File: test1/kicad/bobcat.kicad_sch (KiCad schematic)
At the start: 9 parts, among them U1 Bobcat

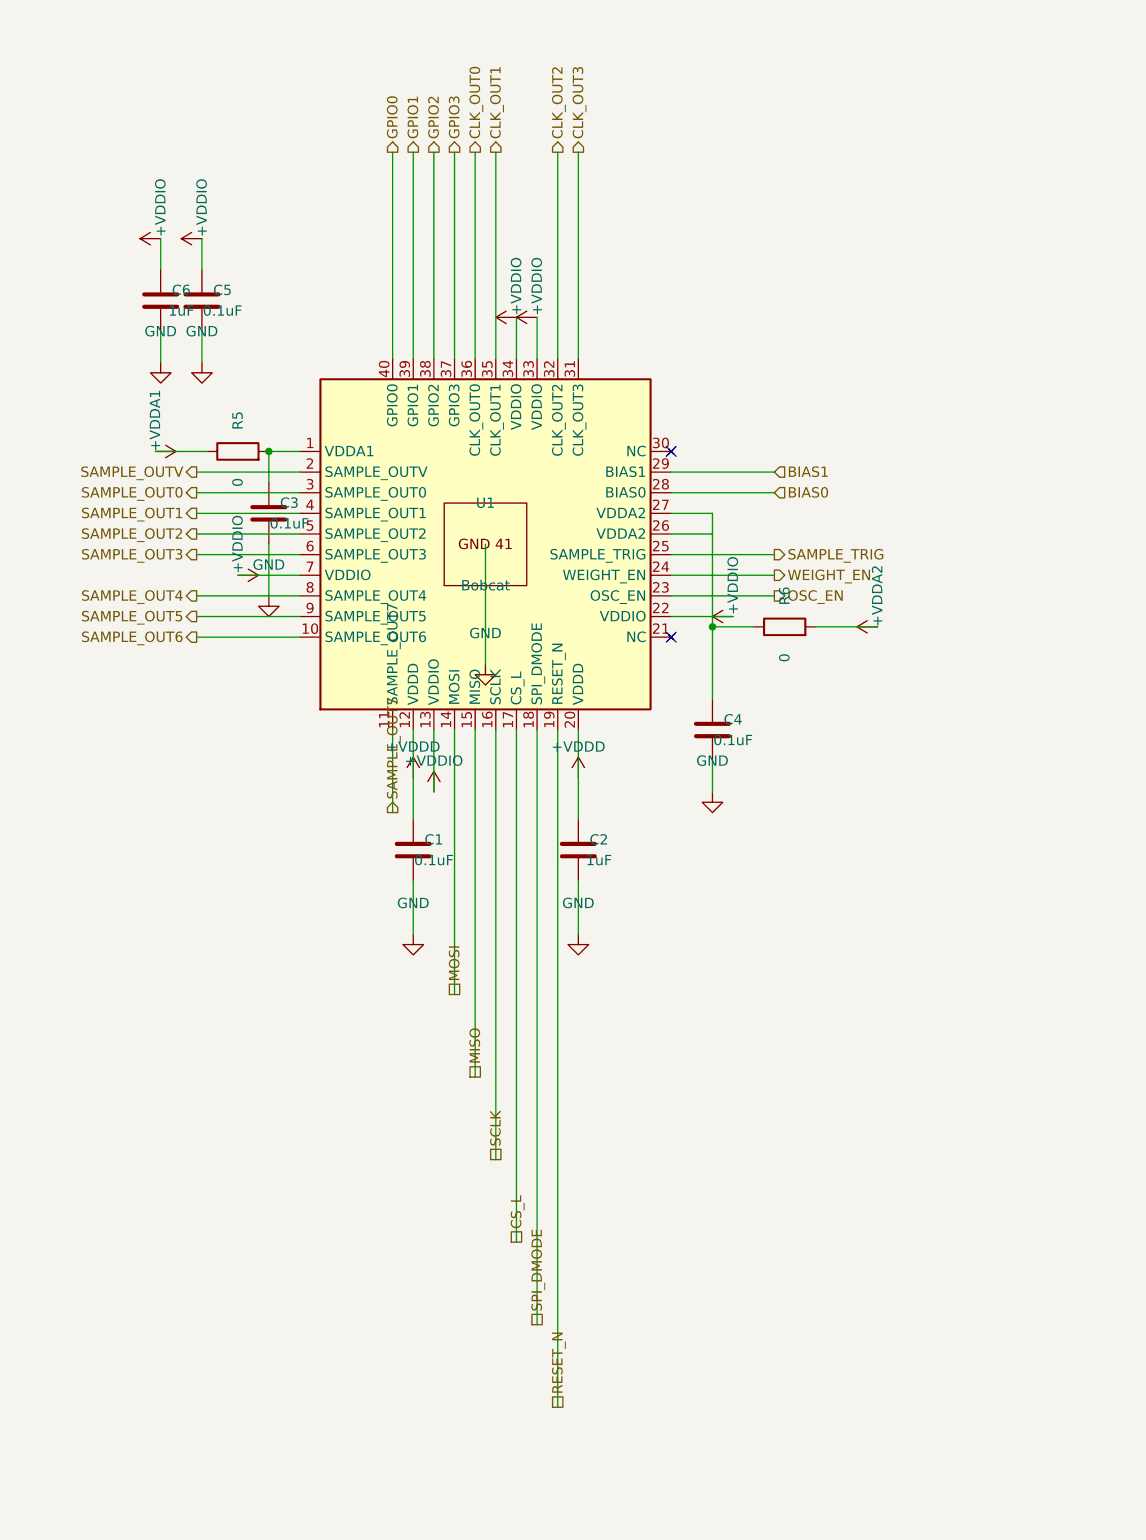
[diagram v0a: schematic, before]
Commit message: Project-wide connectivity audit: refdes uniqueness + hier-label correctness
Added test1/verify_project.py as a kicad-cli-erc substitute (the dev
build doesn't ship _cvpcb.kiface, so sch erc is broken). The verifier
parses all .kicad_sch files and checks:
  1. Duplicate refdes (KiCad's refdes namespace is project-wide).
  2. Parent sheet-pin name + direction matches child hierarchical_label.
  3. Orphan child hierarchical_labels (no matching parent pin).

First run flagged 48 issues. Now reports 0.

Refdes scheme — per-sheet decade ranges so global namespace stays unique:
  FMC 1-9 (J1-J4)
  Power 10-19 (U10/U11, R10/R11, C10-C16, J10-J12)
  Bobcat 20-29 (U20, R20/R21, C20-C25)
  EEPROM 30-39 (U30, R30/R31, C30)
  Bias 40-49 (U40/U41 [U41 dual-unit OPA], Q40-Q43, R40/R41, C40-C43)
  Connectors 50-59 (J50-J57, TP50-TP52)

Hierarchical / global label rework:
  - Parent sheet-pin directions corrected to match child labels (was
    flipped on every Bobcat SPI pin and on FMC's LDO_EN/LSW_EN/LDO_PG).
  - Bobcat SPI labels: passive → input/output as appropriate.
  - Project-wide nets converted to global_label (auto-tie by name, no
    parent pins): SCL, SDA, SAMPLE_OUT*, OSC_EN, WEIGHT_EN, SAMPLE_TRIG,
    BIAS_ISO0/1, CS_L, SCLK, MOSI, MISO, SPI_DMODE, RESET_N.
  - hier_label retained for clean 2-sheet pairs: VADJ, LDO_EN, LDO_PG,
    LSW_EN (FMC ↔ Power); BIAS0/1 (Bias ↔ Bobcat); CLK_OUT0-3, GPIO0-3
    (Bobcat ↔ Connectors).
  - Visual cue in renders: globals render as boxed rectangles; hierarchical
    labels render as arrows — handy when scanning a sheet.

Memory: appended five connectivity-correctness lessons to
feedback_kicad_generator_lessons.md (refdes namespace, parent/child
direction parity, no-passive-for-real-signals, global vs hier decision
table, verify-after-every-change).

Co-Authored-By: Claude Opus 4.7 (1M context) <noreply@anthropic.com>
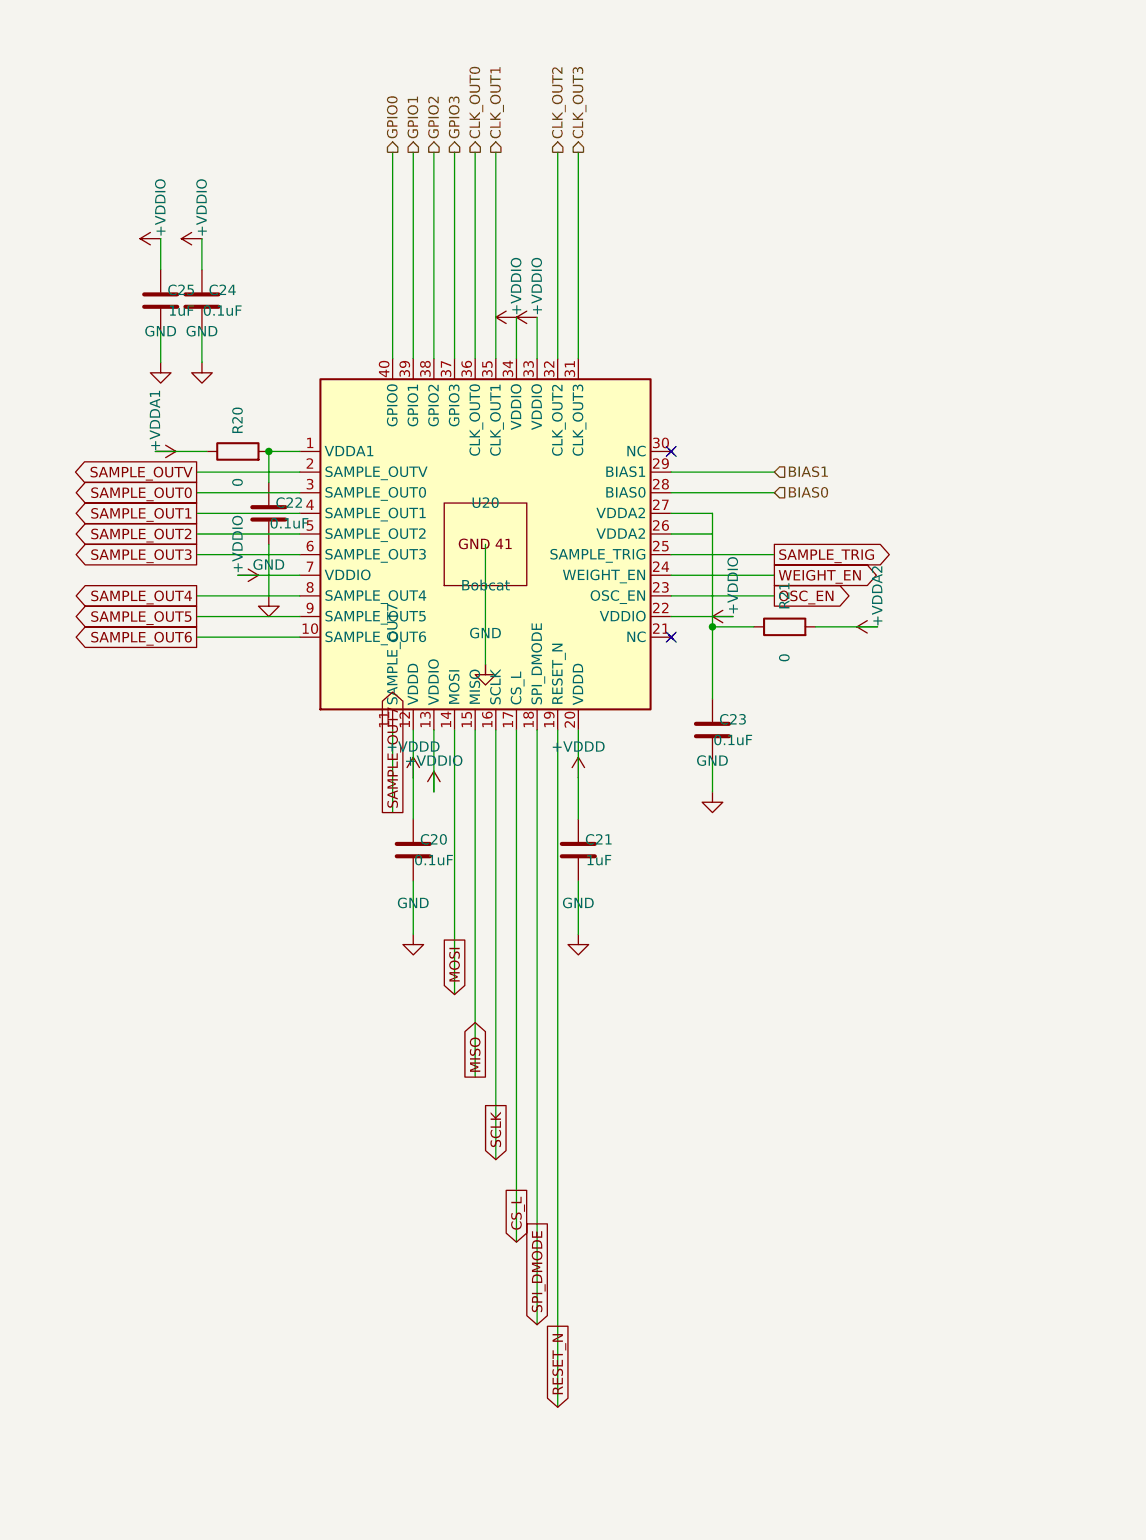
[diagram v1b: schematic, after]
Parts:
- removed C1, C3, C4, C5: 0.1uF, Capacitor_SMD:C_0402_1005Metric, symbol Device:C
- removed C2, C6: 1uF, Capacitor_SMD:C_0402_1005Metric, symbol Device:C
- removed R5, R6: 0, Resistor_SMD:R_0402_1005Metric, symbol Device:R
- removed U1: Bobcat, Bobcat:QFN-40_5x5mm_P0.4mm_EP3.5mm, symbol Lib:Bobcat
- added C20, C22, C23, C24: 0.1uF, Capacitor_SMD:C_0402_1005Metric, symbol Device:C
- added C21, C25: 1uF, Capacitor_SMD:C_0402_1005Metric, symbol Device:C
- added R20, R21: 0, Resistor_SMD:R_0402_1005Metric, symbol Device:R
- added U20: Bobcat, Bobcat:QFN-40_5x5mm_P0.4mm_EP3.5mm, symbol Lib:Bobcat
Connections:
- net +VDDA1: now also R20.1
- net +VDDA2: now also R21.2
- net +VDDD: now also C20.1, C21.1, U20.12 (VDDD), U20.20 (VDDD)
- net +VDDIO: now also C24.1, C25.1, U20.13 (VDDIO), U20.22 (VDDIO), U20.33 (VDDIO), U20.34 (VDDIO), U20.7 (VDDIO)
- net BIAS0: now also U20.28 (BIAS0)
- net BIAS1: now also U20.29 (BIAS1)
- net CLK_OUT0: now also U20.36 (CLK_OUT0)
- net CLK_OUT1: now also U20.35 (CLK_OUT1)
- net CLK_OUT2: now also U20.32 (CLK_OUT2)
- net CLK_OUT3: now also U20.31 (CLK_OUT3)
- net CS_L: now also U20.17 (CS_L)
- net GND: now also C20.2, C21.2, C22.2, C23.2, C24.2, C25.2, U20.41 (GND)
- net GPIO0: now also U20.40 (GPIO0)
- net GPIO1: now also U20.39 (GPIO1)
- net GPIO2: now also U20.38 (GPIO2)
- net GPIO3: now also U20.37 (GPIO3)
- net MISO: now also U20.15 (MISO)
- net MOSI: now also U20.14 (MOSI)
- net OSC_EN: now also U20.23 (OSC_EN)
- net RESET_N: now also U20.19 (RESET_N)
- net SAMPLE_OUT0: now also U20.3 (SAMPLE_OUT0)
- net SAMPLE_OUT1: now also U20.4 (SAMPLE_OUT1)
- net SAMPLE_OUT2: now also U20.5 (SAMPLE_OUT2)
- net SAMPLE_OUT3: now also U20.6 (SAMPLE_OUT3)
- net SAMPLE_OUT4: now also U20.8 (SAMPLE_OUT4)
- net SAMPLE_OUT5: now also U20.9 (SAMPLE_OUT5)
- net SAMPLE_OUT6: now also U20.10 (SAMPLE_OUT6)
- net SAMPLE_OUT7: now also U20.11 (SAMPLE_OUT7)
- net SAMPLE_OUTV: now also U20.2 (SAMPLE_OUTV)
- net SAMPLE_TRIG: now also U20.25 (SAMPLE_TRIG)
- net SCLK: now also U20.16 (SCLK)
- net SPI_DMODE: now also U20.18 (SPI_DMODE)
- net WEIGHT_EN: now also U20.24 (WEIGHT_EN)
- new net: C22.1, R20.2, U20.1 (VDDA1)
- new net: C23.1, R21.1, U20.26 (VDDA2), U20.27 (VDDA2)

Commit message: Split test1 generator into per-sheet package with netlist YAML + strict validator
Combines three layered changes:

1. Apply the design-review audit (test1/error_log.md): 9 ERRORs + 10
   WARNINGs from the new .claude/skills/design_review.md skill — FMC
   LA-bank 0Ω routing, Bobcat SPI/control/GPIO pull network, LDO
   ANY-OUT to FPGA, LDO_PG pull-up + series, bias DNP convention,
   kelvin SNS, per-pin VDDIO + bulk caps, BIAS bypass, VADJ/VDDIO bulk,
   MCP4728 EEPROM provisioning notes, shared-rail decision documented.

2. Refactor test1/gen_schematic.py (1825 lines → 138-line entry point)
   into a per-sheet package at test1/gen/:
     config.py / symbols.py / shared.py  — primitives, Sheet container,
     LA_ASSIGN, footprints, sexpr emit
     build_<sheet>.py × 7                — one builder per child sheet
     netlist.py / validator.py           — YAML loader + strict checker
   Per-session context for any single sheet drops to ~500 lines.
   Also sorts non-deterministic set iteration that made fmc.kicad_sch
   diff noisily across runs.

3. Add a declarative connectivity layer (netlist/<sheet>.yaml):
   parts inventory + nets (power / hier / global / internal), with
   explicit unit syntax for multi-unit symbols (U41:u2.7, J3:u3.G16).
   The strict validator runs at the end of every build_<sheet>() call:
     - inventory: YAML parts ↔ placed (refdes, unit) parity
     - connectivity: every YAML net member is in a connected component
       named the YAML net name (Union-Find on wires + junctions + label
       anchors + power-symbol pins; T-intersections auto-connect)
     - internal nets: members in one component, no name check
   Sheet now records structured PlacedPart/wire/label data alongside
   the s-expr emit; validator reads those instead of re-parsing.

All 6 child sheets' .kicad_sch outputs are byte-identical to the
post-design-review reference, and verify_project.py reports 0 issues.

Co-Authored-By: Claude Opus 4.7 (1M context) <noreply@anthropic.c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
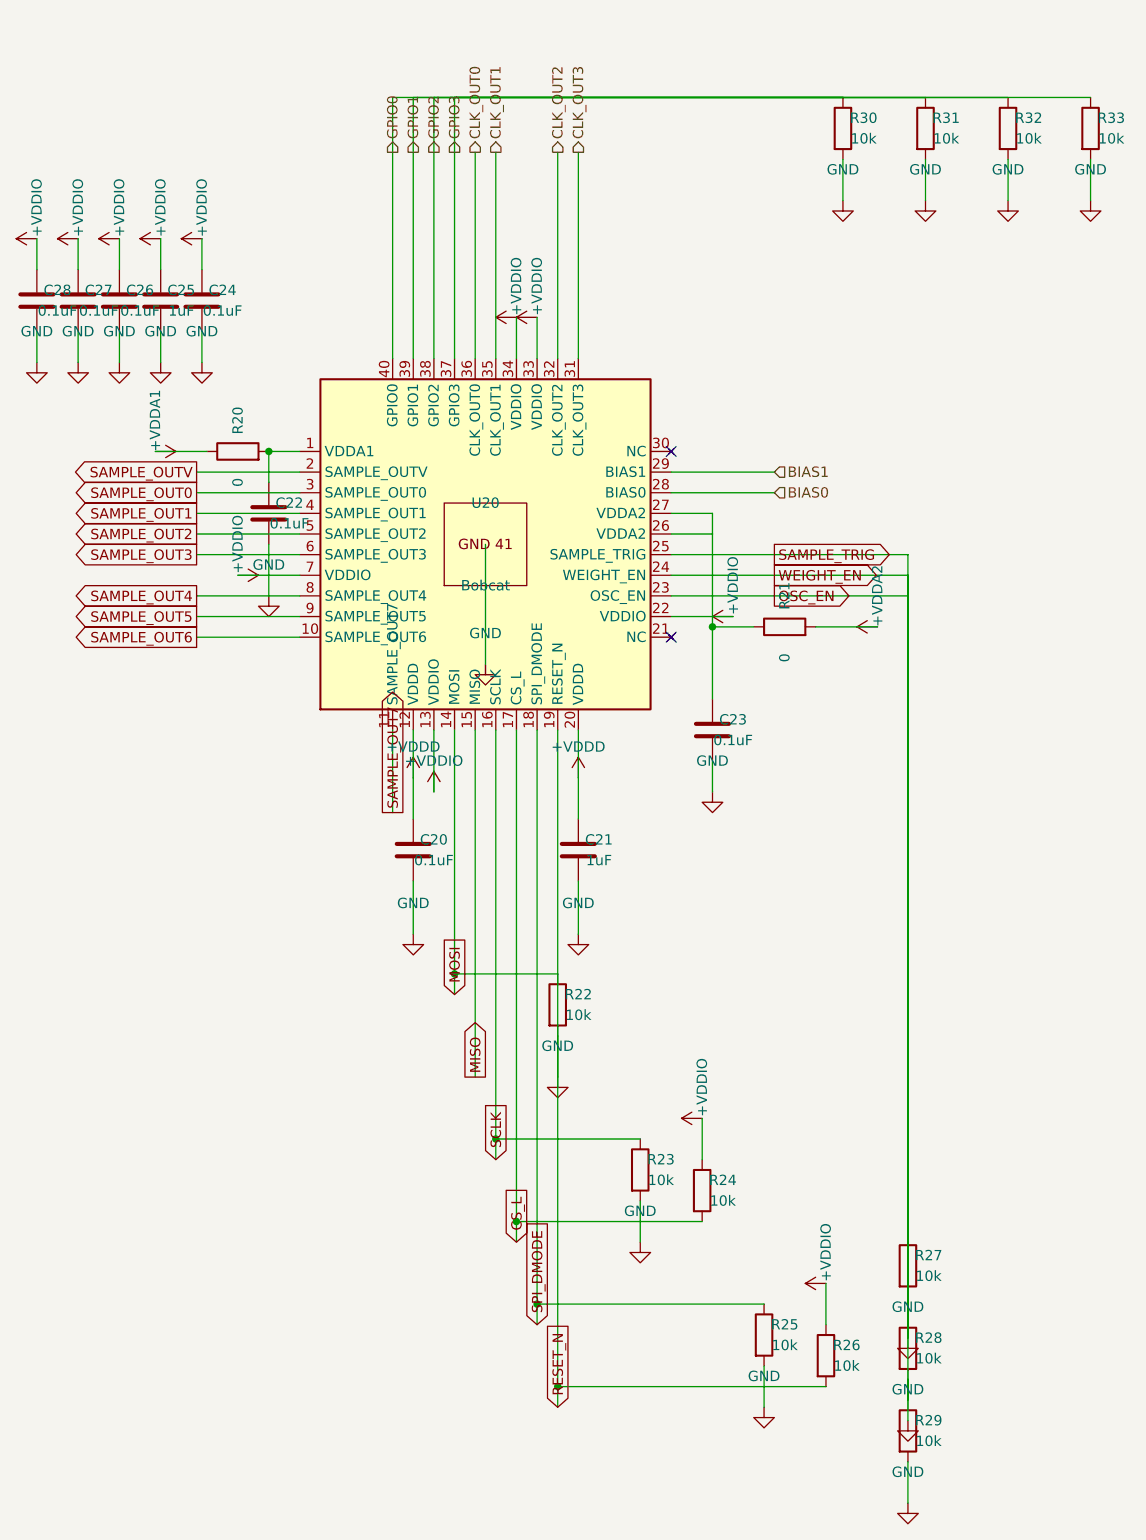
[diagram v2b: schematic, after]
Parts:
- added C26, C27, C28: 0.1uF, Capacitor_SMD:C_0402_1005Metric, symbol Device:C
- added R22, R23, R24, R25, R26, R27, R28, R29, R30, R31, R32, R33: 10k, Resistor_SMD:R_0402_1005Metric, symbol Device:R
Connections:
- net GPIO1 is gone; now on net GPIO0: U20.39 (GPIO1)
- net GPIO2 is gone; now on net GPIO0: U20.38 (GPIO2)
- net GPIO3 is gone; now on net GPIO0: U20.37 (GPIO3)
- net OSC_EN is gone; now on net GND: U20.23 (OSC_EN)
- net RESET_N is gone; now on net GND: U20.19 (RESET_N)
- net SAMPLE_TRIG is gone; now on net GND: U20.25 (SAMPLE_TRIG)
- net WEIGHT_EN is gone; now on net GND: U20.24 (WEIGHT_EN)
- net +VDDIO: now also C26.1, C27.1, C28.1, R24.1, R26.1
- net CS_L: now also R24.2
- net GND: now also C26.2, C27.2, C28.2, R22.2, R23.2, R25.2, R26.2, R27.1, R27.2, R28.1, R28.2, R29.1, R29.2, R30.2, R31.2, R32.2, R33.2
- net GPIO0: now also R30.1, R31.1, R32.1, R33.1
- net MOSI: now also R22.1
- net SCLK: now also R23.1
- net SPI_DMODE: now also R25.1
